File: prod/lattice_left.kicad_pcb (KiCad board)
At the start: 2 copper layers, 114.3 x 85.7 mm, 84 parts

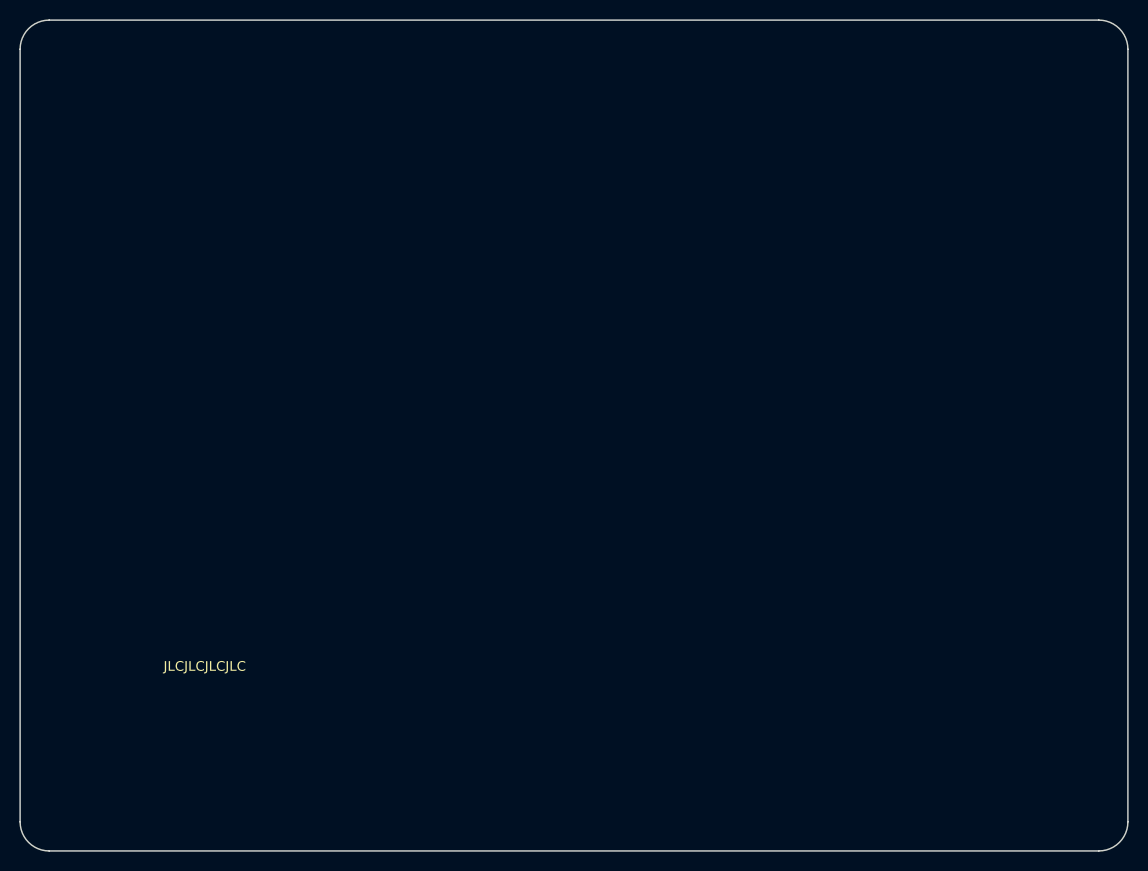
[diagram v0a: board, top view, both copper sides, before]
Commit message: preoject-specific 3dmodels and footprints
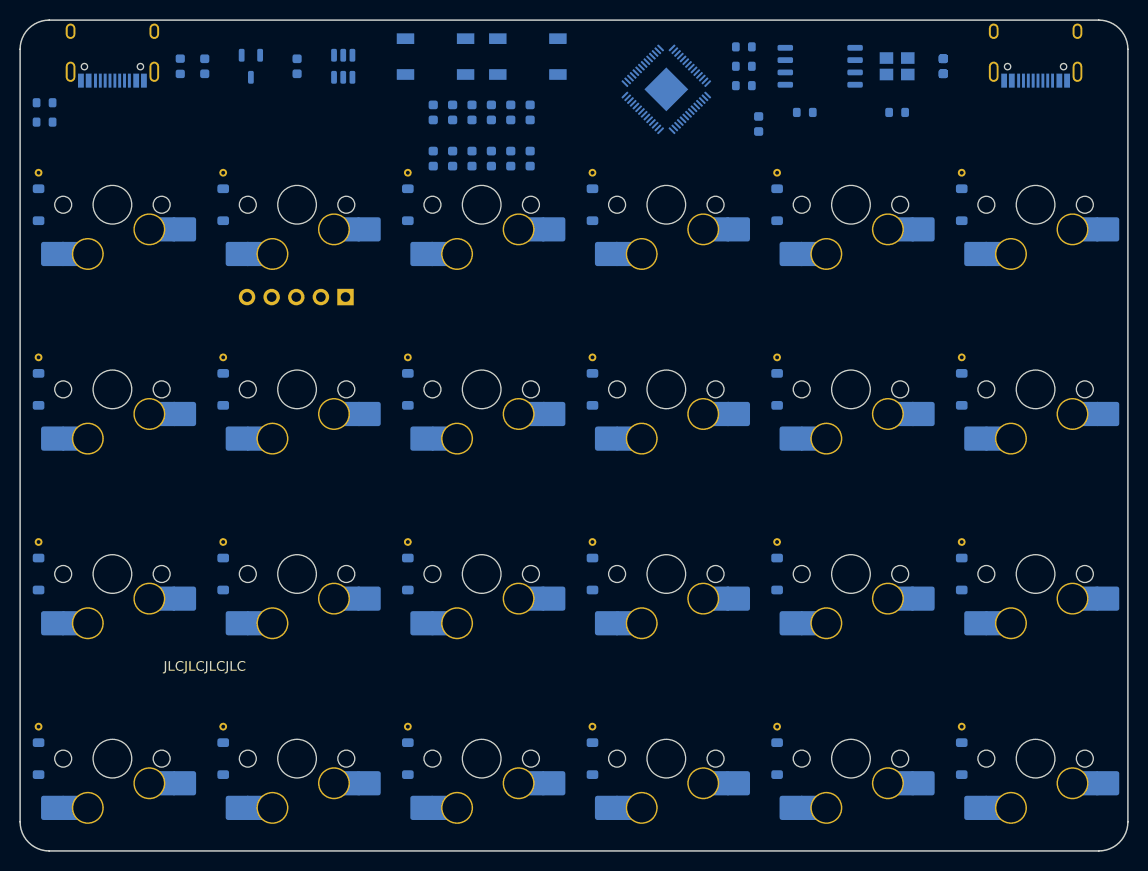
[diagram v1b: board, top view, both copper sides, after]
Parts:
- C1, C15, C2, C7: value (none) -> 1uF; footprint 1uF -> Capacitor_SMD:C_0603_1608Metric
- C10, C11, C12, C13, C14, C16, C17, C8, C9: value (none) -> 100nF; footprint 100nF -> Capacitor_SMD:C_0603_1608Metric
- C3: value (none) -> 100nf; footprint 100nF -> Capacitor_SMD:C_0603_1608Metric
- C4, C5: value (none) -> 22pF; footprint 22pF -> Capacitor_SMD:C_0603_1608Metric
- C6: value (none) -> 10uF; footprint 10uF -> Capacitor_SMD:C_0603_1608Metric
- D1, D10, D11, D12, D13, D14, D15, D16, D17, D18, D19, D2, D20, D21, D22, D23, D24, D3, D4, D5, D6, D7, D8, D9: value (none) -> 1N4148W; footprint 1N4148W -> lattice:D_SOD-123_via
- F1: value (none) -> 500mA; footprint 500mA -> Fuse:Fuse_0603_1608Metric
- J1, J2: value (none) -> USB_C_Receptacle; footprint USB_C_Receptacle -> lattice:USB_C_Receptacle_HRO_TYPE-C-31-M-12
- J3: value (none) -> Conn_01x05; footprint Conn_01x05 -> lattice:PinHeader_1x05_P2.54mm_Vertical
- MX1, MX10, MX11, MX12, MX13, MX14, MX15, MX16, MX17, MX18, MX19, MX2, MX20, MX21, MX22, MX23, MX24, MX3, MX4, MX5, MX6, MX7, MX8, MX9: value (none) -> MX_SW_HS; footprint MX_SW_HS -> lattice:SW_MX_HS_1u
- R1, R2: value (none) -> 5k1; footprint 5k1 -> Resistor_SMD:R_0603_1608Metric
- R3, R4: value (none) -> 27R; footprint 27R -> Resistor_SMD:R_0603_1608Metric
- R5, R6, R7: value (none) -> 1k; footprint 1k -> Resistor_SMD:R_0603_1608Metric
- SW1, SW2: value (none) -> SW_Push; footprint SW_Push -> lattice:SW_SPST_SKQG_WithStem
- SYM1: value (none) -> Logo_Open_Hardware_Small; footprint Logo_Open_Hardware_Small -> Symbol:OSHW-Logo_5.7x6mm_SilkScreen
- U1: value (none) -> RP2040; footprint RP2040 -> Package_DFN_QFN:QFN-56-1EP_7x7mm_P0.4mm_EP3.2x3.2mm
- U2: value (none) -> XC6206PxxxMR; footprint W25Q128JVS -> lattice:SOT-23-3
- U3: value (none) -> USBLC6-2SC6; footprint USBLC6-2SC6 -> Package_TO_SOT_SMD:SOT-23-6
- U4: value (none) -> W25Q128JVS; footprint XC6206PxxxMR -> lattice:SOIC-8_5.23x5.23mm_P1.27mm
- Y1: value (none) -> 12MHz; footprint 12MHz -> Crystal:Crystal_SMD_3225-4Pin_3.2x2.5mm
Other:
- net class Default removed

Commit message: component placement
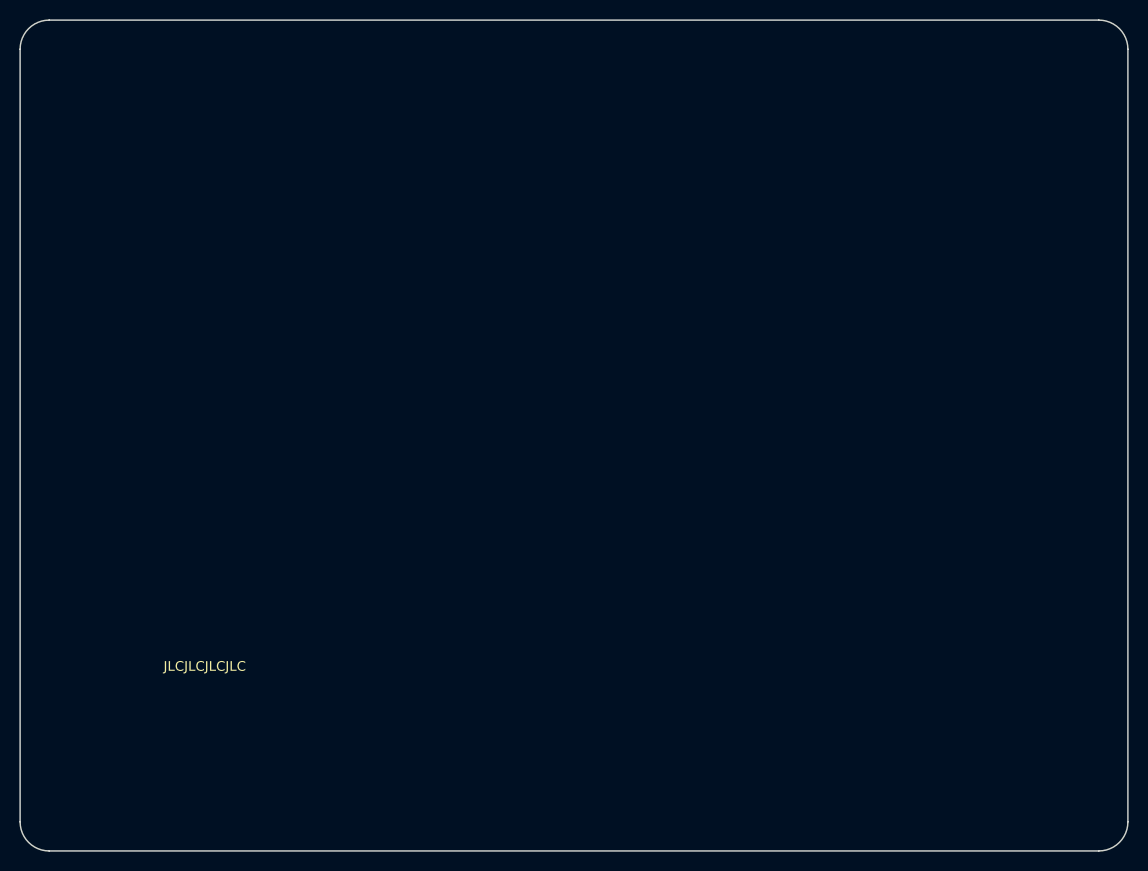
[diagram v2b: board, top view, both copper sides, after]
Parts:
- C1, C15, C2, C7: value 1uF -> (none); footprint Capacitor_SMD:C_0603_1608Metric -> 1uF
- C10, C11, C12, C13, C14, C16, C17, C8, C9: value 100nF -> (none); footprint Capacitor_SMD:C_0603_1608Metric -> 100nF
- C3: value 100nf -> (none); footprint Capacitor_SMD:C_0603_1608Metric -> 100nF
- C4, C5: value 22pF -> (none); footprint Capacitor_SMD:C_0603_1608Metric -> 22pF
- C6: value 10uF -> (none); footprint Capacitor_SMD:C_0603_1608Metric -> 10uF
- D1, D10, D11, D12, D13, D14, D15, D16, D17, D18, D19, D2, D20, D21, D22, D23, D24, D3, D4, D5, D6, D7, D8, D9: value 1N4148W -> (none); footprint lattice:D_SOD-123_via -> 1N4148W
- F1: value 500mA -> (none); footprint Fuse:Fuse_0603_1608Metric -> 500mA
- J1, J2: value USB_C_Receptacle -> (none); footprint lattice:USB_C_Receptacle_HRO_TYPE-C-31-M-12 -> USB_C_Receptacle
- J3: value Conn_01x05 -> (none); footprint lattice:PinHeader_1x05_P2.54mm_Vertical -> Conn_01x05
- MX1, MX10, MX11, MX12, MX13, MX14, MX15, MX16, MX17, MX18, MX19, MX2, MX20, MX21, MX22, MX23, MX24, MX3, MX4, MX5, MX6, MX7, MX8, MX9: value MX_SW_HS -> (none); footprint lattice:SW_MX_HS_1u -> MX_SW_HS
- R1, R2: value 5k1 -> (none); footprint Resistor_SMD:R_0603_1608Metric -> 5k1
- R3, R4: value 27R -> (none); footprint Resistor_SMD:R_0603_1608Metric -> 27R
- R5, R6, R7: value 1k -> (none); footprint Resistor_SMD:R_0603_1608Metric -> 1k
- SW1, SW2: value SW_Push -> (none); footprint lattice:SW_SPST_SKQG_WithStem -> SW_Push
- SYM1: value Logo_Open_Hardware_Small -> (none); footprint Symbol:OSHW-Logo_5.7x6mm_SilkScreen -> Logo_Open_Hardware_Small
- U1: value RP2040 -> (none); footprint Package_DFN_QFN:QFN-56-1EP_7x7mm_P0.4mm_EP3.2x3.2mm -> RP2040
- U2: value XC6206PxxxMR -> (none); footprint lattice:SOT-23-3 -> W25Q128JVS
- U3: value USBLC6-2SC6 -> (none); footprint Package_TO_SOT_SMD:SOT-23-6 -> USBLC6-2SC6
- U4: value W25Q128JVS -> (none); footprint lattice:SOIC-8_5.23x5.23mm_P1.27mm -> XC6206PxxxMR
- Y1: value 12MHz -> (none); footprint Crystal:Crystal_SMD_3225-4Pin_3.2x2.5mm -> 12MHz
- moved R3 15.0 mm to (145.4, 40.9)
- moved R4 15.0 mm to (145.4, 42.9)
- moved R5 15.0 mm to (145.4, 44.9)
- moved C3 9.52 mm to (171.4, 48.8)
- moved U1 3.18 mm to (155.6, 45.2)
- moved C5 2.00 mm to (183.0, 42.9)
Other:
- net class Default added: clearance 0.2, trace_width 0.25, via_dia 0.8, via_drill 0.4
